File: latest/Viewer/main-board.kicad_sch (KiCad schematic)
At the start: 66 parts, among them J1 USB_C_Receptacle_USB2.0_16P, J2 S4B-XH-A_LF__SN_, J3 S4B-XH-A_LF__SN_, J4 Conn_ARM_JTAG_SWD_10, Q1 AONR21307, U1 HUSB238_xxxDD, U2 AP63205WU, U3 AP2112K-3.3, U4 PTR54L, U5 TMC2226-SA, U6 TMC2226-SA, U7 KTD2026BEWE-TR

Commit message: Update latest build (main@ecd6afb)
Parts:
- removed C27: EEE-FT1V101AP, EEE1AA101SP, symbol Samacsys:EEE-FT1V101AP
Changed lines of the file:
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@@
-    (stroke (width 0) (type default))
-  )
-  (wire (pts (xy 363.22 147.32) (xy 375.92 147.32))
     (stroke (width 0) (type default))
   )
@@
   )
   (wire (pts (xy 307.34 46.99) (xy 313.69 46.99))
-    (stroke (width 0) (type default))
-  )
-  (wire (pts (xy 363.22 160.02) (xy 375.92 160.02))
     (stroke (width 0) (type default))
   )
@@
         )
       )
-    )
-  )
-  (symbol (lib_id "Samacsys:EEE-FT1V101AP") (at 375.92 160.02 90) (unit 1) (body_style 1)
-    (exclude_from_sim no) (in_bom yes) (on_board yes) (in_pos_files yes) (dnp no) (fields_autoplaced)
-    (property "Reference" "C27" (at 379.73 152.3999 90) (do_not_autoplace no) (show_name no)
-      (effects (font (size 1.27 1.27)) (justify right))
-    )
-    (property "Value" "EEE-FT1V101AP" (at 379.73 154.9399 90) (do_not_autoplace no) (show_name no)
-      (effects (font (size 1.27 1.27)) (justify right))
-    )
-    (property "Footprint" "EEE1AA101SP" (at 472.11 151.13 0) (do_not_autoplace no) (show_name no) (hide yes)
-      (effects (font (size 1.27 1.27)) (justify left top))
-    )
-    (property "Datasheet" "http://industrial.panasonic.com/cdbs/www-data/pdf/RDE0000/ABA0000C1240.pdf" (at 572.11 151.13 0) (do_not_autoplace no) (show_name no) (hide yes)
-      (effects (font (size 1.27 1.27)) (justify left top))
-    )
-    (property "Description" "Aluminum Electrolytic Capacitors - SMD 100uF 35volts 6.3x5.8mm SMD" (at 375.92 160.02 0) (do_not_autoplace no) (show_name no) (hide yes)
-      (effects (font (size 1.27 1.27)))
-    )
-    (property "Height" "7.8" (at 772.11 151.13 0) (do_not_autoplace no) (show_name no) (hide yes)
-      (effects (font (size 1.27 1.27)) (justify left top))
-    )
-    (property "Manufacturer_Name" "Panasonic" (at 872.11 151.13 0) (do_not_autoplace no) (show_name no) (hide yes)
-      (effects (font (size 1.27 1.27)) (justify left top))
-    )
-    (property "Manufacturer_Part_Number" "EEE-FT1V101AP" (at 972.11 151.13 0) (do_not_autoplace no) (show_name no) (hide yes)
-      (effects (font (size 1.27 1.27)) (justify left top))
-    )
-    (property "Mouser Part Number" "667-EEE-FT1V101AP" (at 1072.11 151.13 0) (do_not_autoplace no) (show_name no) (hide yes)
-      (effects (font (size 1.27 1.27)) (justify left top))
-    )
-    (property "Mouser Price/Stock" "https://www.mouser.co.uk/ProductDetail/Panasonic/EEE-FT1V101AP?qs=CMJjuEs1%252BuEsbOqam%2FkTqg%3D%3D" (at 1172.11 151.13 0) (do_not_autoplace no) (show_name no) (hide yes)
-      (effects (font (size 1.27 1.27)) (justify left top))
-    )
-    (property "Arrow Part Number" "EEE-FT1V101AP" (at 1272.11 151.13 0) (do_not_autoplace no) (show_name no) (hide yes)
-      (effects (font (size 1.27 1.27)) (justify left top))
-    )
-    (property "Arrow Price/Stock" "https://www.arrow.com/en/products/eeeft1v101ap/panasonic.html?utm_currency=USD&region=nac" (at 1372.11 151.13 0) (do_not_autoplace no) (show_name no) (hide yes)
-      (effects (font (size 1.27 1.27)) (justify left top))
-    )
-    (pin "2")
-    (pin "1")
-    (instances
-      (project "main-board"
-        (path "/fe215afa-a228-4dbb-8560-a0753323a3f2"
-          (reference "C27") (unit 1)
-        )
-      )

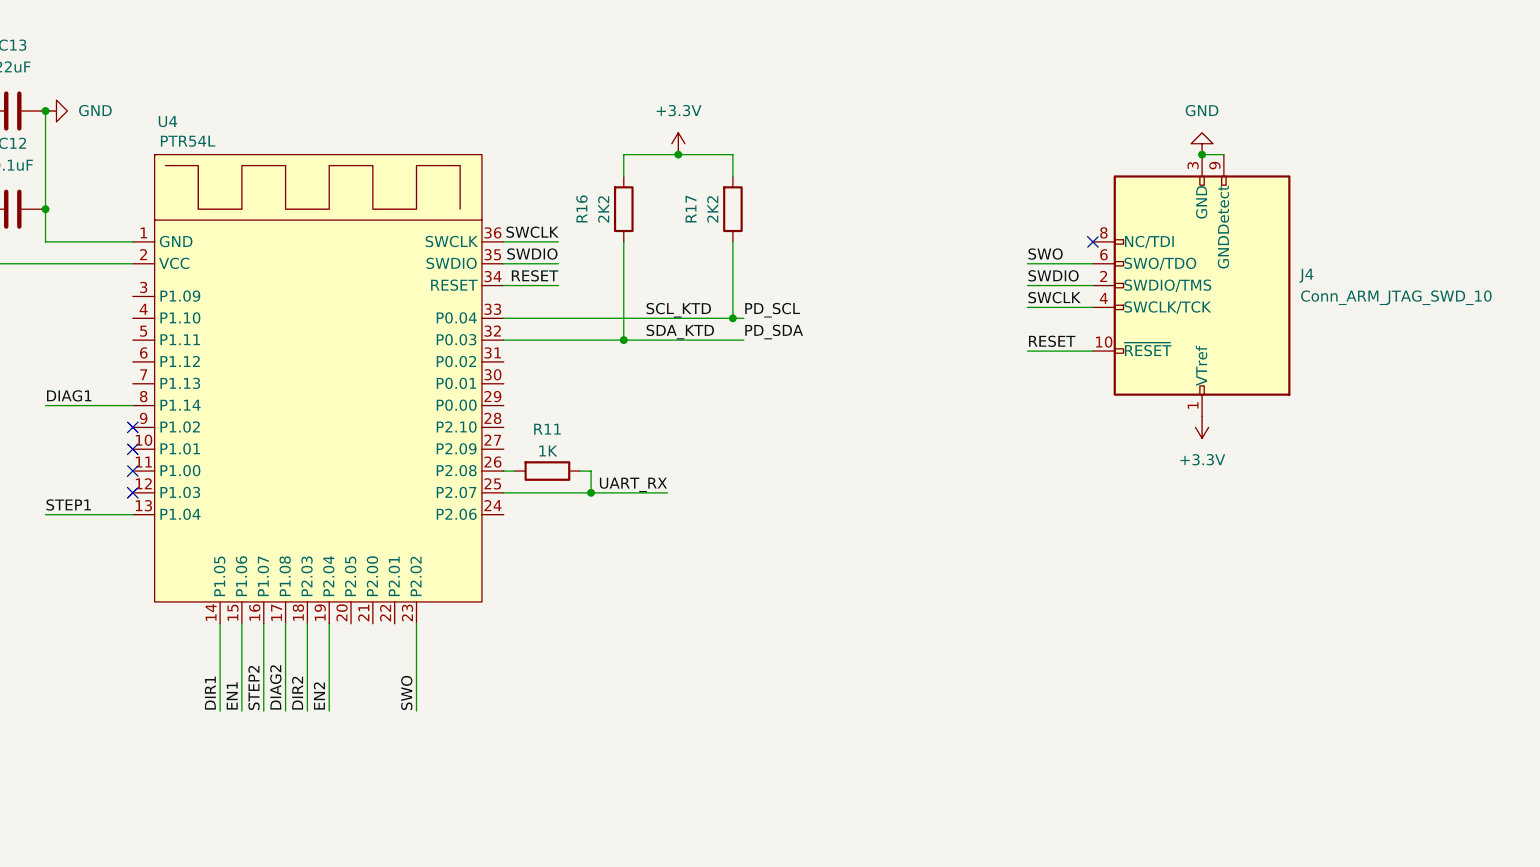
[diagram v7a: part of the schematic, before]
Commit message: Update latest build (main@b81b70f)
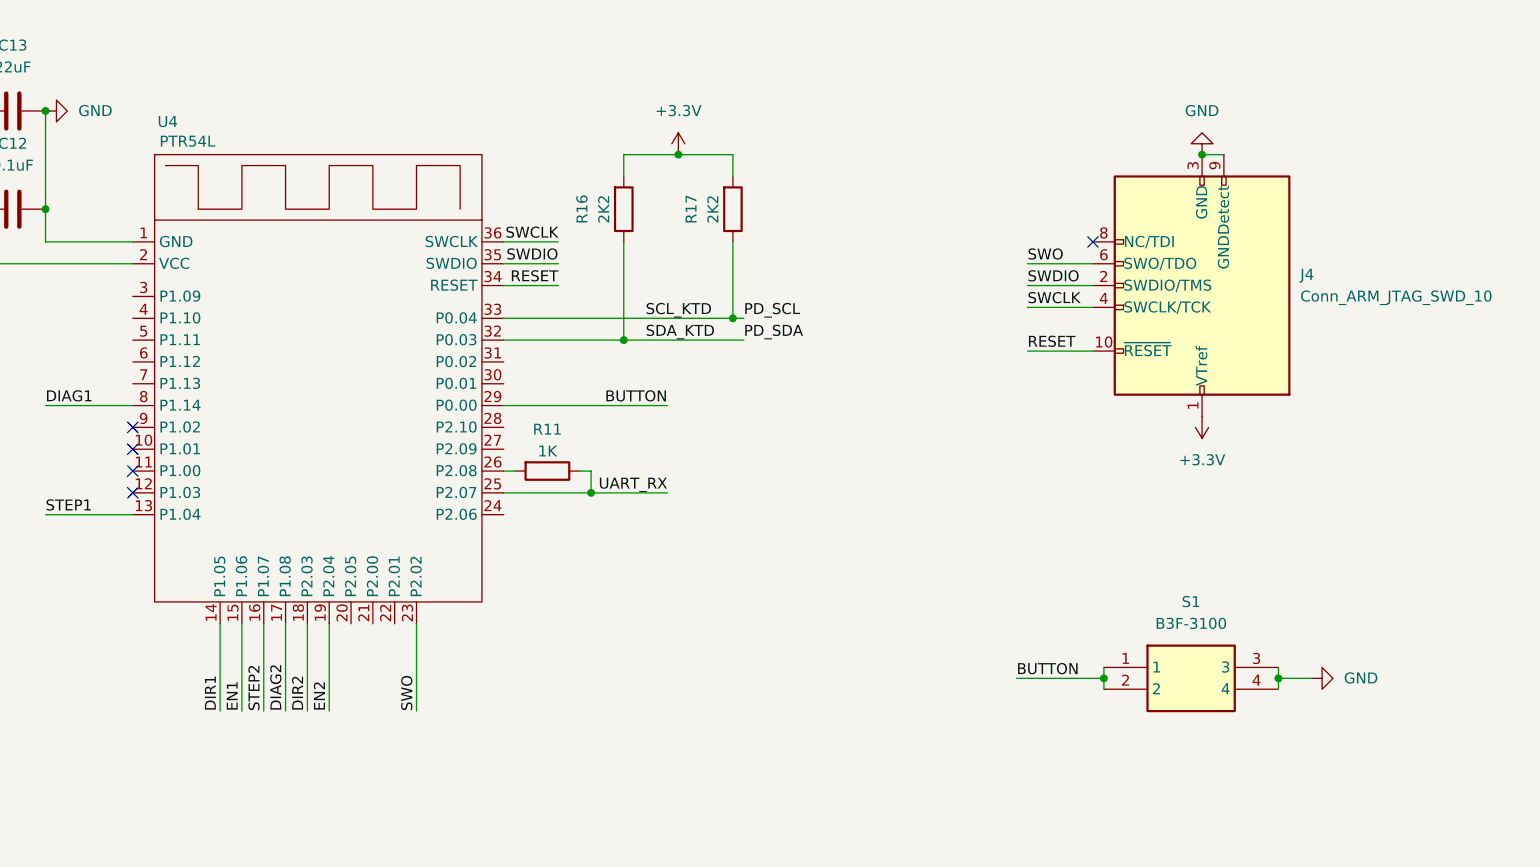
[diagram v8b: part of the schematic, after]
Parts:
- added S1: B3F-3100, B3F3100, symbol Samacsys:B3F-3100
- J2: footprint Samacsys:S4BXHALFSN -> S4BXHALFSN
- L1: footprint Samacsys:INDPM4441X200N -> INDPM4441X200N
- Q1: footprint Samacsys:DFN_3X3_EP -> DFN_3X3_EP
- U7: footprint Project_Specific_Parts:UTDFN8_1P5X1P5_KIN -> UTDFN8_1P5X1P5_KIN
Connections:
- net GND: now also S1.3, S1.4
- net BUTTON: now reaches U4.29 (P0.00)
- net BUTTON: now also S1.1, S1.2
